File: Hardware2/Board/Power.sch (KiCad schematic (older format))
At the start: 40 parts, among them J7 Jumper, P20 TP, P21 TP, P22 TP, P23 TP, P24 2060-452, P25 2060-452, P26 TP, P27 TP, P28 2060-452, P29 2059-302, P30 LED_Strip, P31 LED_Strip, P35 2060-452, U5 TPS82130, U6 LP2985IM5-3.3, U7 TPS82130, U8 SP485CN, U9 TPS82130

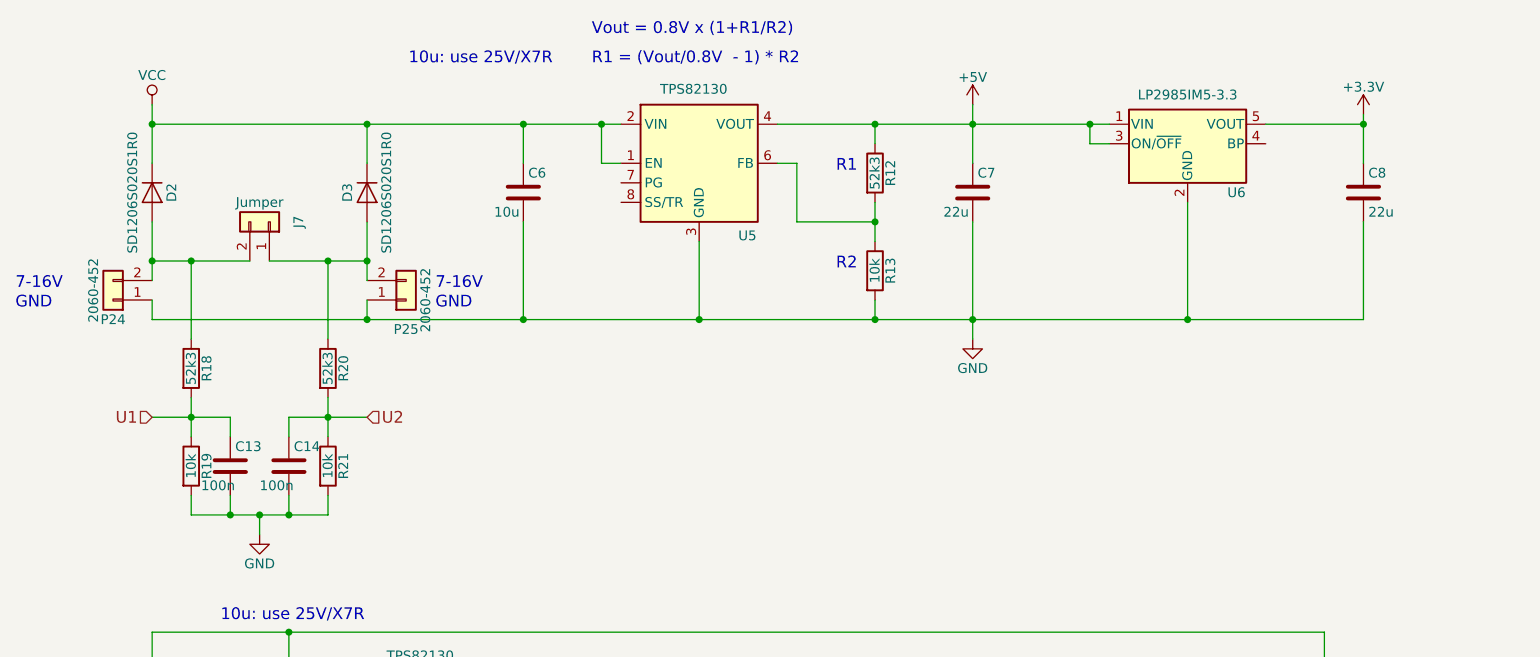
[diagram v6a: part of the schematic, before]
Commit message: add rfid and speaker
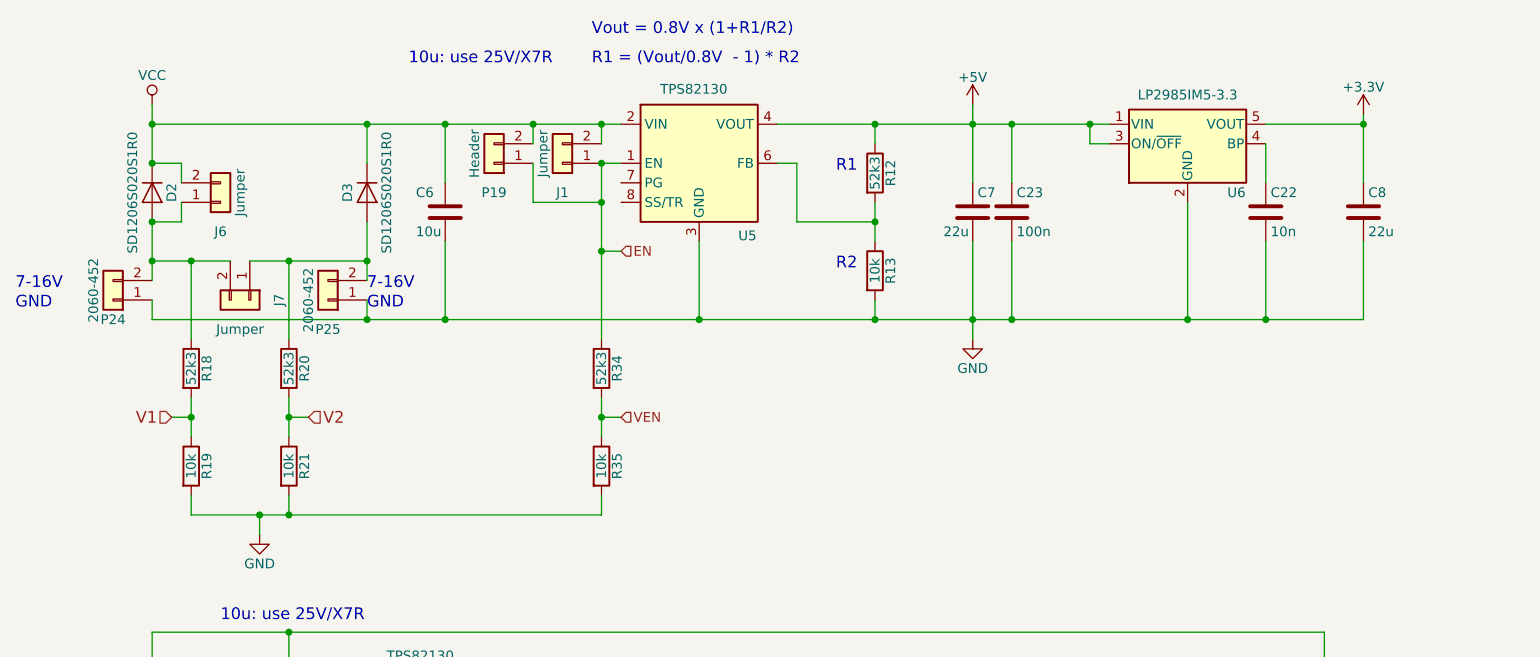
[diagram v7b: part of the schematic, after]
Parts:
- removed C13, C14: 100n, Capacitor_SMD:C_0603_1608Metric, symbol Device:C
- added C22: 10n, Capacitor_SMD:C_0603_1608Metric, symbol Device:C
- added C23: 100n, Capacitor_SMD:C_0603_1608Metric, symbol Device:C
- added J1, J6: Jumper, LedControl:Jumper, symbol Connector_Generic:Conn_01x02
- added P19: Header, Connector_PinHeader_2.54mm:PinHeader_1x02_P2.54mm_Vertical, symbol Connector_Generic:Conn_01x02
- added R34: 52k3, Resistor_SMD:R_0603_1608Metric, symbol Device:R
- added R35: 10k, Resistor_SMD:R_0603_1608Metric, symbol Device:R
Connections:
- net +5V: now also C23.1
- net GND: now also C22.2, C23.2, R35.2
- net VCC: now also J1.2 (Pin_2), J6.2 (Pin_2), P19.2 (Pin_2); no longer U5.1 (EN)
- net at U6.4 (BP): now also C22.1
- net at D2.2 (A), J7.2 (Pin_2), P24.2 (Pin_2)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: now also J6.1 (Pin_1)
- net U1 renamed V1
- net U2 renamed V2
- new net EN: J1.1 (Pin_1), P19.1 (Pin_1), R34.1, U5.1 (EN)
- new net VEN: R34.2, R35.1
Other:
- moved on the sheet: C6, C7, C8, J7, P25, R20, R21
